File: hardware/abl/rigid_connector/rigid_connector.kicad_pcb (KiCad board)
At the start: 2 copper layers, 53.5 x 29.1 mm, 6 parts, among them J1 009159008603906, J2 009159008603906

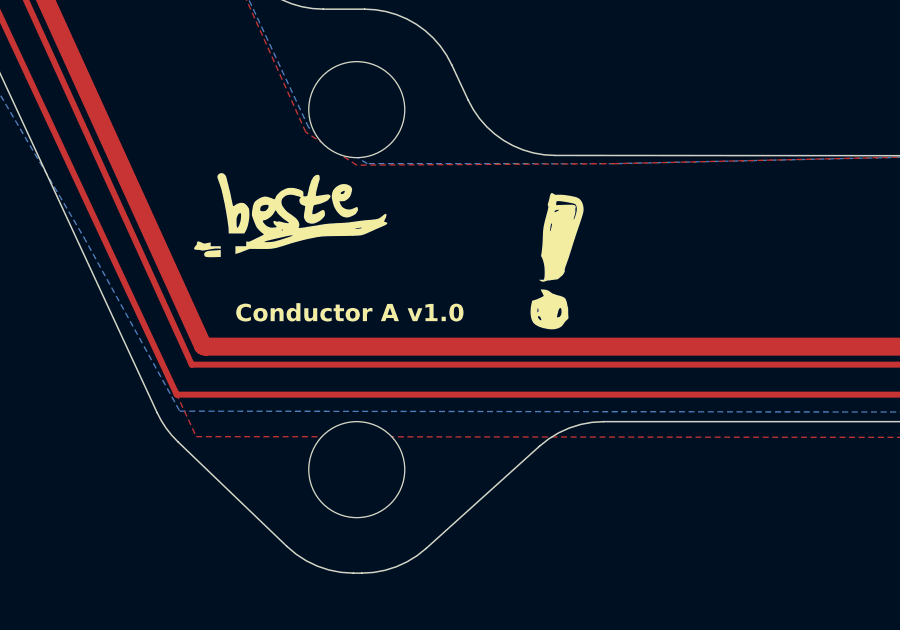
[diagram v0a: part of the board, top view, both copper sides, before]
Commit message: Rename files, names and labels to be more consistent. Add READMEs for connectors and extend some other READMEs.
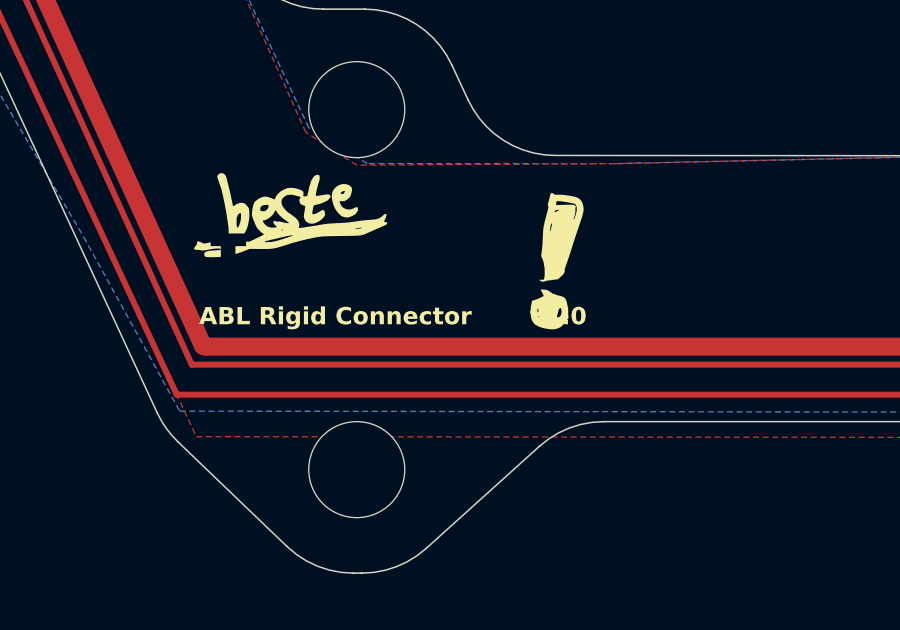
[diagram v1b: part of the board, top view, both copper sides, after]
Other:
- board text added: "ABL Rigid Connector v1.0"
- board text removed: "Conductor A v1.0"

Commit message: Many small adjustments for the next production run.
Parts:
- moved H1 13.2 mm to (77.0, 85.0)
- moved H2 13.1 mm to (77.0, 94.0)
- moved G*** 3.84 mm to (95.1, 88.7)
- moved J2 1.71 mm to (76.5, 74.5)
- moved G*** 1.66 mm to (92.4, 88.7)
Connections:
- J1 pad 2: /VLED -> /5V
- J1 pad 4: /VLED -> /5V
- J2 pad 6: /VLED -> /5V
- J2 pad 8: /VLED -> /5V
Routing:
- net /5V: track 61.0 -> 0.00 mm
- net /GND: track 0.00 -> 50.5 mm, vias 0 -> 5
- net /SDA: track 61.9 -> 60.2 mm
- added copper zone on F.Cu, net /5V
- removed copper zone on F.Cu, net /VLED
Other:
- board size 53.5 x 29.1 mm -> 54 x 28.6 mm
- board text added: "5V"
- board text added: "ABL Rigid Connector v1.1"
- board text added: "GND"
- board text added: "SCL"
- board text added: "SDA"
- board text added: "https://beste-lampe.de"
- board text removed: "ABL Rigid Connector v1.0"
- board text removed: "https://lenaschimmel.de/besteLampe!"
